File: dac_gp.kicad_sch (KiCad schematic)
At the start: 11 parts

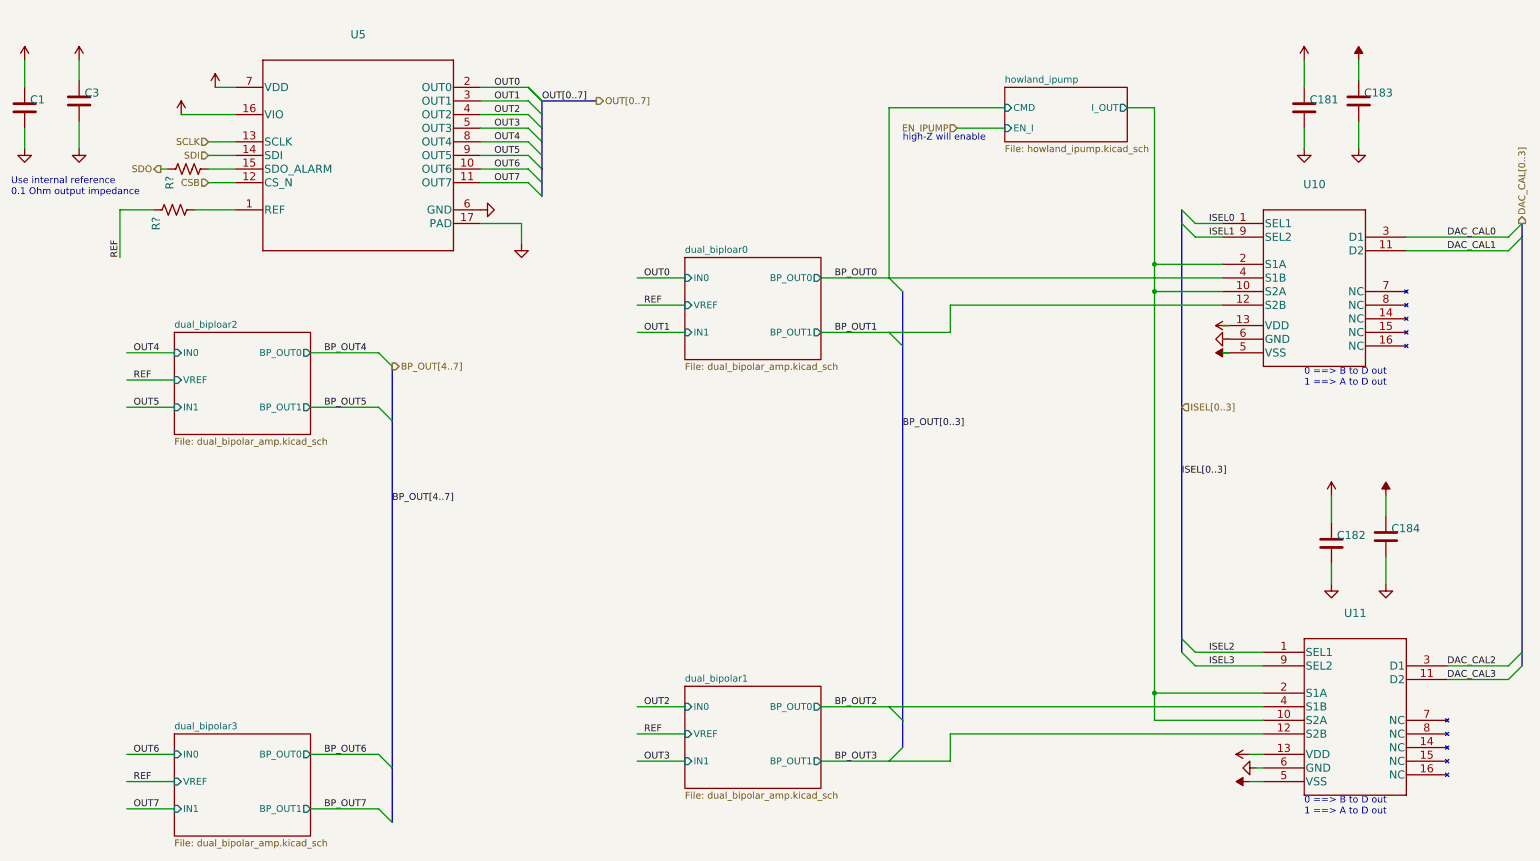
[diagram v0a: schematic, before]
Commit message: closes #31 - incorrect text on Howland current pump. Also, updated fast DAC symbol but not closing until layout is corrected
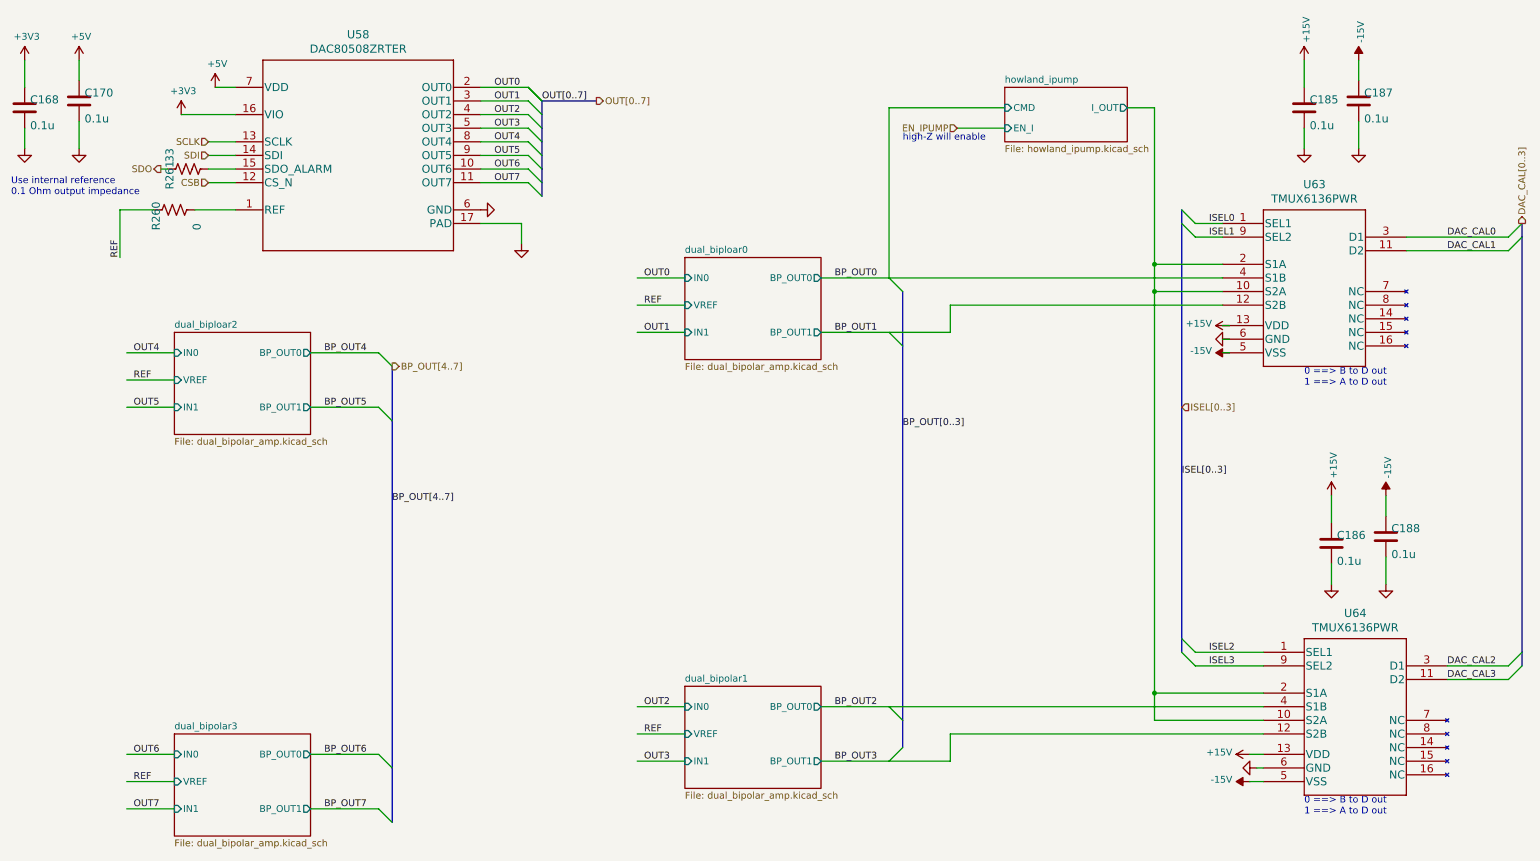
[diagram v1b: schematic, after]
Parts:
- C168: renamed from C1; value (none) -> 0.1u; footprint (none) -> Capacitor_SMD:C_0603_1608Metric
- C170: renamed from C3; value (none) -> 0.1u; footprint (none) -> Capacitor_SMD:C_0603_1608Metric
- C185: renamed from C181; value (none) -> 0.1u; footprint (none) -> Capacitor_SMD:C_0603_1608Metric
- C186: renamed from C182; value (none) -> 0.1u; footprint (none) -> Capacitor_SMD:C_0603_1608Metric
- C187: renamed from C183; value (none) -> 0.1u; footprint (none) -> Capacitor_SMD:C_0603_1608Metric
- C188: renamed from C184; value (none) -> 0.1u; footprint (none) -> Capacitor_SMD:C_0603_1608Metric
- R260: renamed from R?; value (none) -> 0; footprint (none) -> Resistor_SMD:R_0603_1608Metric
- R261: renamed from R?; value (none) -> 33; footprint (none) -> Resistor_SMD:R_0603_1608Metric
- U58: renamed from U5; value (none) -> DAC80508ZRTER; footprint (none) -> Package_DFN_QFN:WQFN-16-1EP_3x3mm_P0.5mm_EP1.6x1.6mm
- U63: renamed from U10; value (none) -> TMUX6136PWR; footprint (none) -> Package_SO:TSSOP-16_4.4x5mm_P0.65mm
- U64: renamed from U11; value (none) -> TMUX6136PWR; footprint (none) -> Package_SO:TSSOP-16_4.4x5mm_P0.65mm
